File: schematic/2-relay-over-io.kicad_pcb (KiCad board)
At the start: 2 copper layers, 86.4 x 51.4 mm, 26 parts, among them J1 Conn_02x08_Odd_Even, J2 Conn_02x08_Odd_Even, Q2 BC817, Q3 BC817, U1 SONGLE_3V_relay, U2 SONGLE_3V_relay, U6 DizzyBITLogo, U7 DizzyBIT-Layout

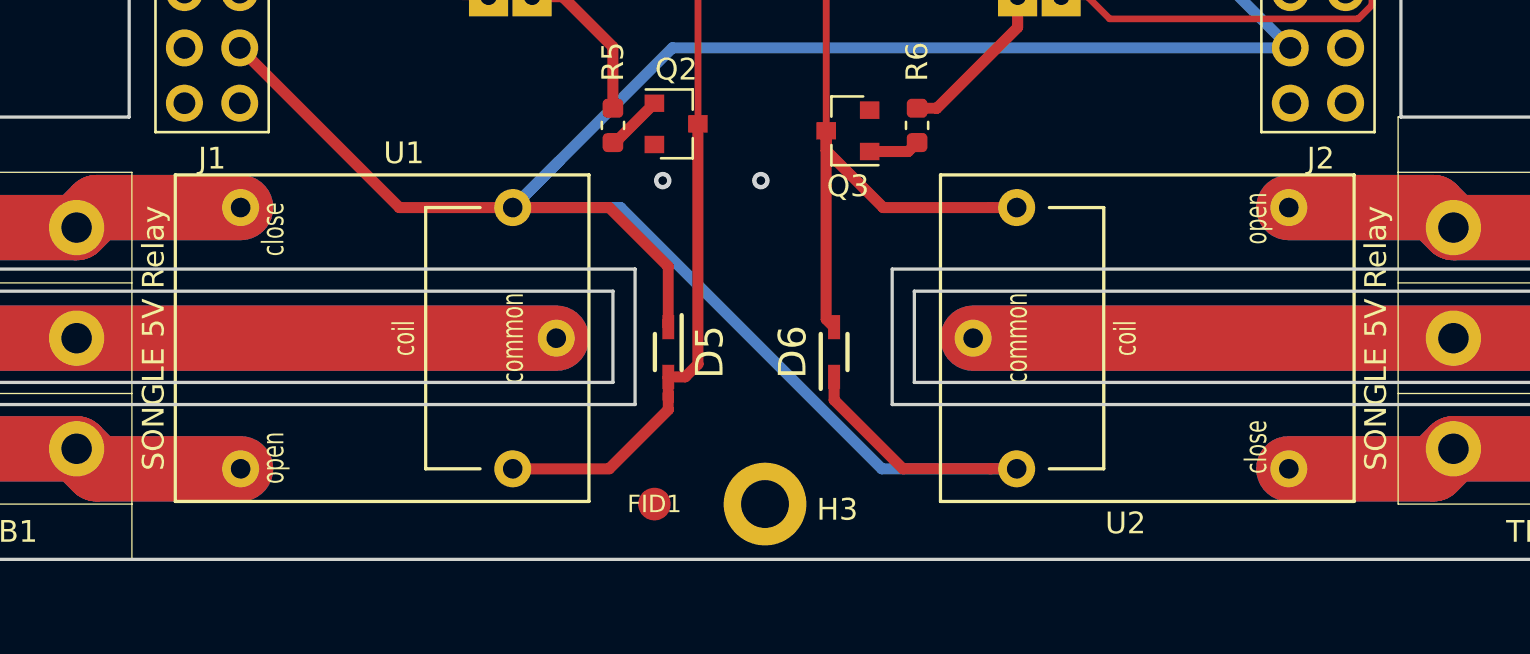
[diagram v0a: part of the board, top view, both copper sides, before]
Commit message: Changed the relay footprint to have bigger holes
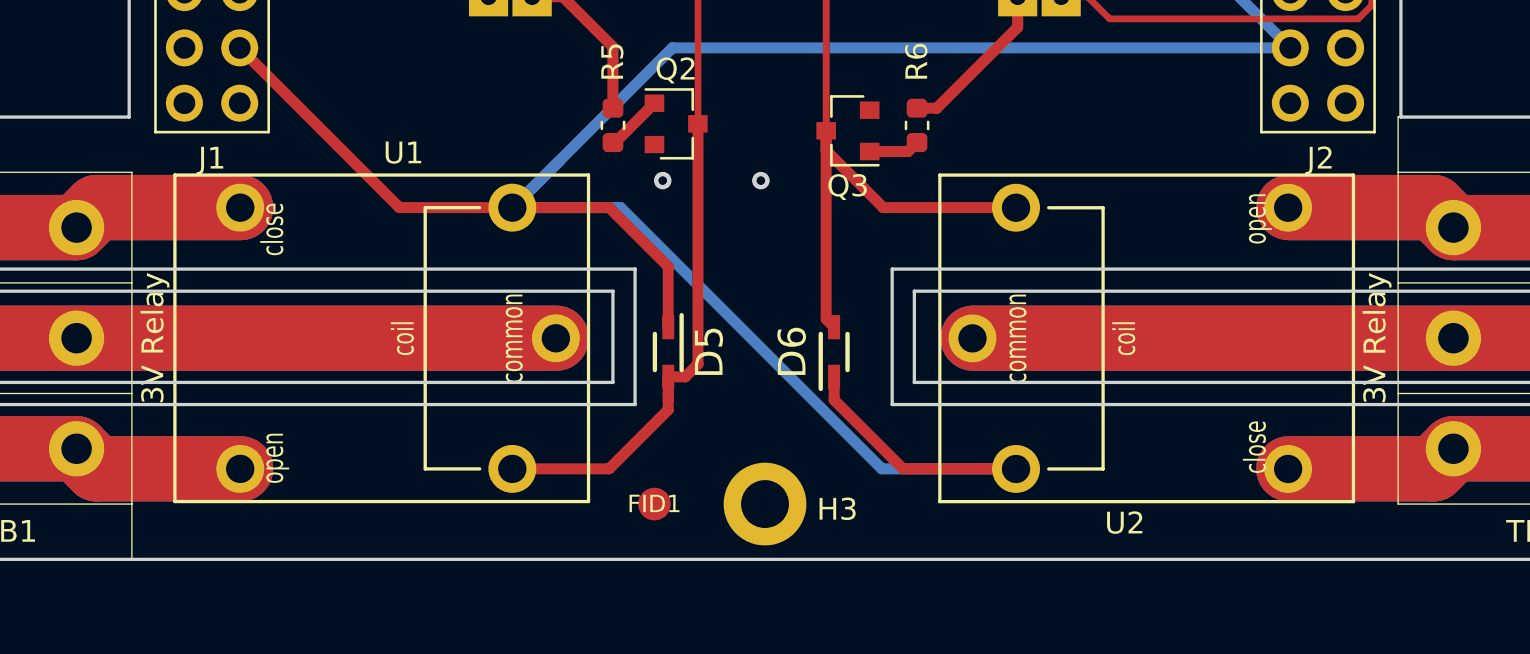
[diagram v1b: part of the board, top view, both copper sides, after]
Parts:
- U1, U2: footprint Songle:SONGLE_5V_Relay -> Songle:SONGLE_3V_Relay
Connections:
- J1 pad 1: I39 -> (no net)
- J1 pad 2: I36 -> (no net)
- J2 pad 1: VSPI_MOSI -> (no net)
- J2 pad 2: I2C_SCL -> (no net)
- J2 pad 3: IO1 -> (no net)

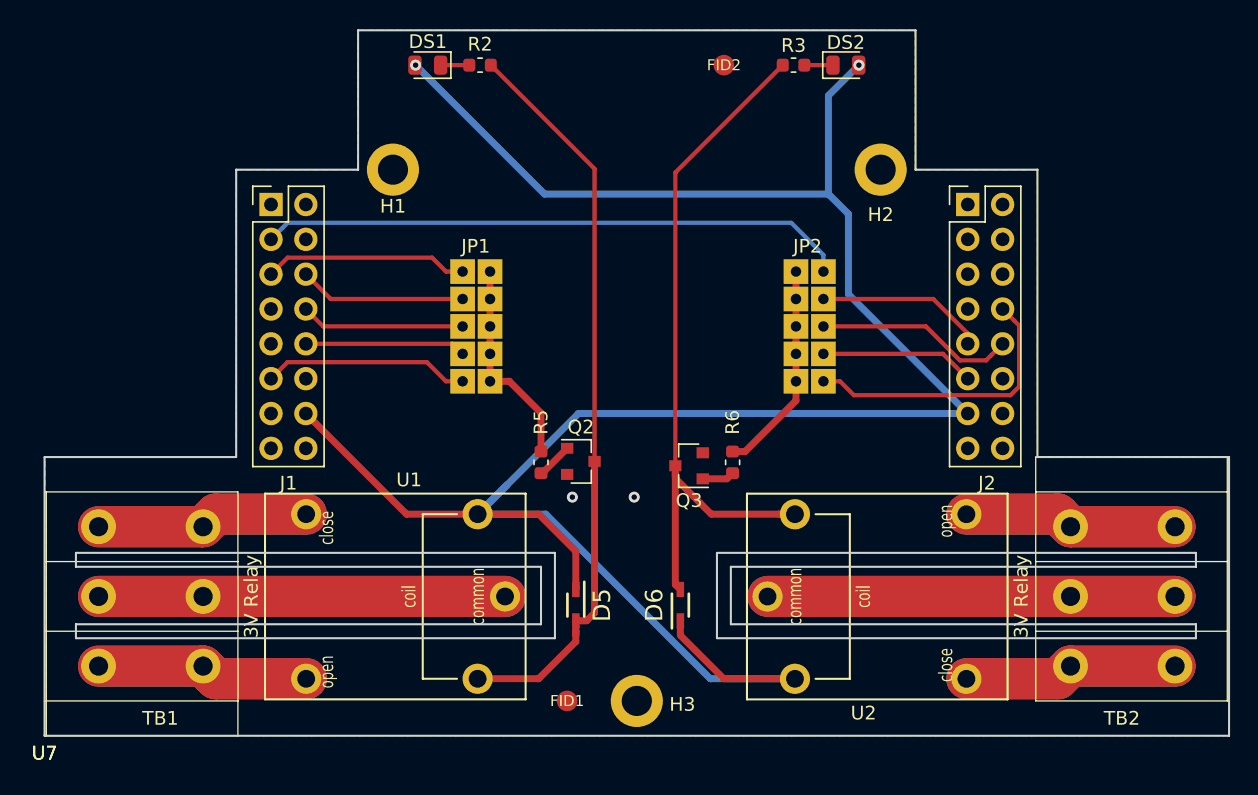
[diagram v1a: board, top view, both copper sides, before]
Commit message: Major Update. Changed pin configuration and board outline. Relays now use the 5V load in order to avoid stressing the regulator.
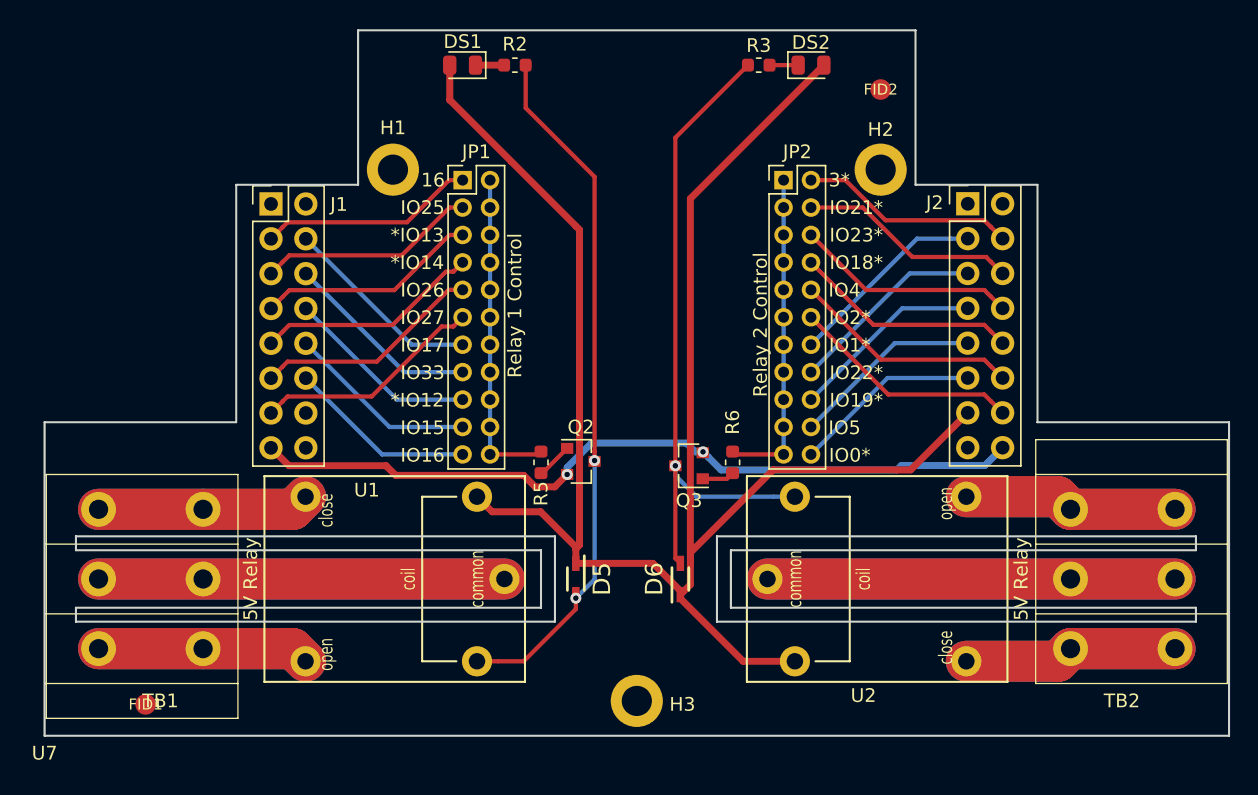
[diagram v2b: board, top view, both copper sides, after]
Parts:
- removed the U7 at (76.2, 146.1) (x2)
- added U7: DizzyBIT-Layout, DizzyBit:DizzyBit-Din Rail Module, F.Cu at (76.2, 146.1)
- JP1, JP2: value Conn_02x05_Odd_Even -> Conn_02x11_Odd_Even; footprint DizzyBit:DizzyBit-SolderJumper-5-5-Open -> Connector_PinHeader_2.00mm:PinHeader_2x11_P2.00mm_Vertical
- U1, U2: value SONGLE_3V_relay -> SONGLE_5V_relay; footprint Songle:SONGLE_3V_Relay -> Songle:SONGLE_5V_Relay
- moved FID1 30.7 mm to (83.6, 143.8)
- moved JP2 16.1 mm to (130.1, 105.5), turned to 0 degrees
- moved FID2 11.6 mm to (137.2, 98.9)
- moved JP1 5.76 mm to (106.7, 105.5)
- moved DS1 2.54 mm to (106.7, 97.2)
- moved DS2 2.54 mm to (132.1, 97.2)
- moved R2 2.54 mm to (110.5, 97.2)
- moved R3 2.54 mm to (128.3, 97.2)
- moved D5 1.91 mm to (114.9, 134.6)
- moved D6 1.91 mm to (122.6, 134.6)
- moved U2 1.28 mm to (136.4, 135.1)
- moved U1 1.28 mm to (102.2, 134.1)
- moved TB1 1.27 mm to (90.3, 144.8)
- moved TB2 1.27 mm to (148.5, 124.5)
- moved J2 0.05 mm to (143.5, 107.3)
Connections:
- D5 pad 1: +3V3 -> EXT_5V
- D6 pad 1: +3V3 -> EXT_5V
- DS1 pad 2: +3V3 -> EXT_5V
- DS2 pad 2: +3V3 -> EXT_5V
- J1 pad 10: IO27 -> IO15
- J1 pad 11: IO15 -> IO26
- J1 pad 12: (no net) -> IO32
- J1 pad 13: (no net) -> IO27
- J1 pad 14: +3V3 -> (no net)
- J1 pad 15: (no net) -> GND
- J1 pad 16: GND -> (no net)
- J1 pad 3: IO33 -> IO16
- J1 pad 4: (no net) -> IO17
- J1 pad 5: IO26 -> IO25
- J1 pad 6: IO32 -> IO33
- J1 pad 7: (no net) -> HSPI_MOSI
- J1 pad 8: IO25 -> HSPI_MISO
- J1 pad 9: (no net) -> HSPI_CLK
- J2 pad 10: IO16 -> VSPI_CLK
- J2 pad 11: IO4 -> IO0
- J2 pad 12: (no net) -> IO4
- J2 pad 13: +3V3 -> EXT_5V
- J2 pad 14: (no net) -> IO2
- J2 pad 15: GND -> (no net)
- J2 pad 16: (no net) -> GND
- J2 pad 3: (no net) -> IO1
- J2 pad 4: (no net) -> IO3
- J2 pad 5: (no net) -> I2C_SCL
- J2 pad 6: (no net) -> I2C_SDA
- J2 pad 7: (no net) -> VSPI_MISO
- J2 pad 8: IO5 -> VSPI_MOSI
- J2 pad 9: IO17 -> IO5
- JP1 pad 1: IO26 -> IO16
- JP1 pad 3: IO32 -> IO25
- JP1 pad 5: IO25 -> HSPI_MOSI
- JP1 pad 7: IO27 -> HSPI_CLK
- JP1 pad 9: IO15 -> IO26
- JP2 pad 1: IO5 -> RELAY2_CTR
- JP2 pad 10: RELAY2_CTR -> IO4
- JP2 pad 2: RELAY2_CTR -> IO3
- JP2 pad 3: IO4 -> RELAY2_CTR
- JP2 pad 4: RELAY2_CTR -> I2C_SDA
- JP2 pad 5: IO16 -> RELAY2_CTR
- JP2 pad 6: RELAY2_CTR -> VSPI_MOSI
- JP2 pad 7: IO17 -> RELAY2_CTR
- JP2 pad 8: RELAY2_CTR -> VSPI_CLK
- JP2 pad 9: IO33 -> RELAY2_CTR
- U1 pad 1: +3V3 -> EXT_5V
- U2 pad 1: +3V3 -> EXT_5V
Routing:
- net +3V3: track 172.4 -> 0.00 mm, vias 2 -> 0
- net EXT_5V: track 0.00 -> 136.8 mm
- net GND: track 0.00 -> 57.5 mm
- net IO33: track 43.0 -> 14.4 mm
- net IO2: track 0.00 -> 16.9 mm
- net HSPI_CLK: track 0.00 -> 16.4 mm
- net VSPI_CLK: track 0.00 -> 16.4 mm
- net HSPI_MOSI: track 0.00 -> 16.2 mm
- net VSPI_MOSI: track 0.00 -> 16.2 mm
- net I2C_SDA: track 0.00 -> 16.0 mm
- net IO3: track 0.00 -> 15.7 mm
- net IO1: track 0.00 -> 14.6 mm
- net I2C_SCL: track 0.00 -> 14.4 mm
- net VSPI_MISO: track 0.00 -> 14.2 mm
- net HSPI_MISO: track 0.00 -> 14.2 mm
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- removed copper zone on B.Cu, net GND
- removed copper zone on F.Cu, net GND
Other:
- outline, holes or cut-outs redrawn
- board text added: "*IO12"
- board text added: "*IO13"
- board text added: "*IO14"
- board text added: "16"
- board text added: "3*"
- board text added: "IO0*"
- board text added: "IO1*"
- board text added: "IO18*"
- board text added: "IO19*"
- board text added: "IO2*"
- board text added: "IO21*"
- board text added: "IO22*"
- board text added: "IO23*"
- board text added: "IO4"
- board text added: "IO5"
- board text added: "V 1.0.1"
- board text removed: "IO04"
- board text removed: "IO05"
- board text removed: "IO32"
